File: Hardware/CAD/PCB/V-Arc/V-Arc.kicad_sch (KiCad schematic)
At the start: 0 parts

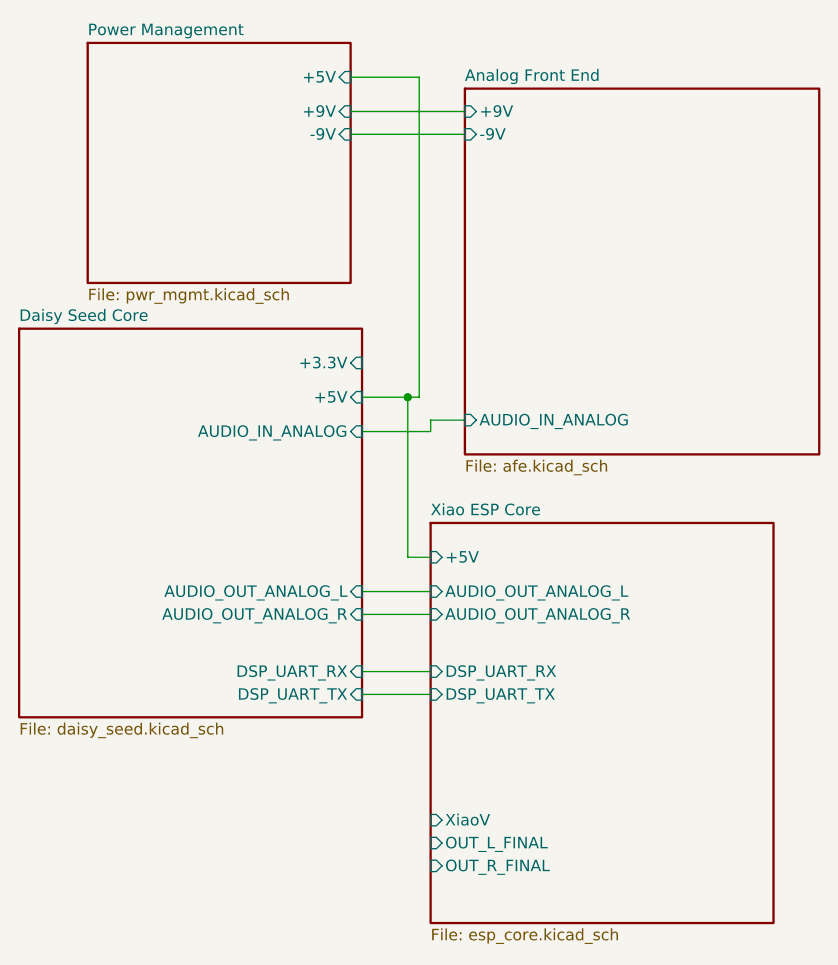
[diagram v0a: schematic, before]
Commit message: Assigned Footprints
-Swapped input jack to a switched one
-Assigned footprints for all items
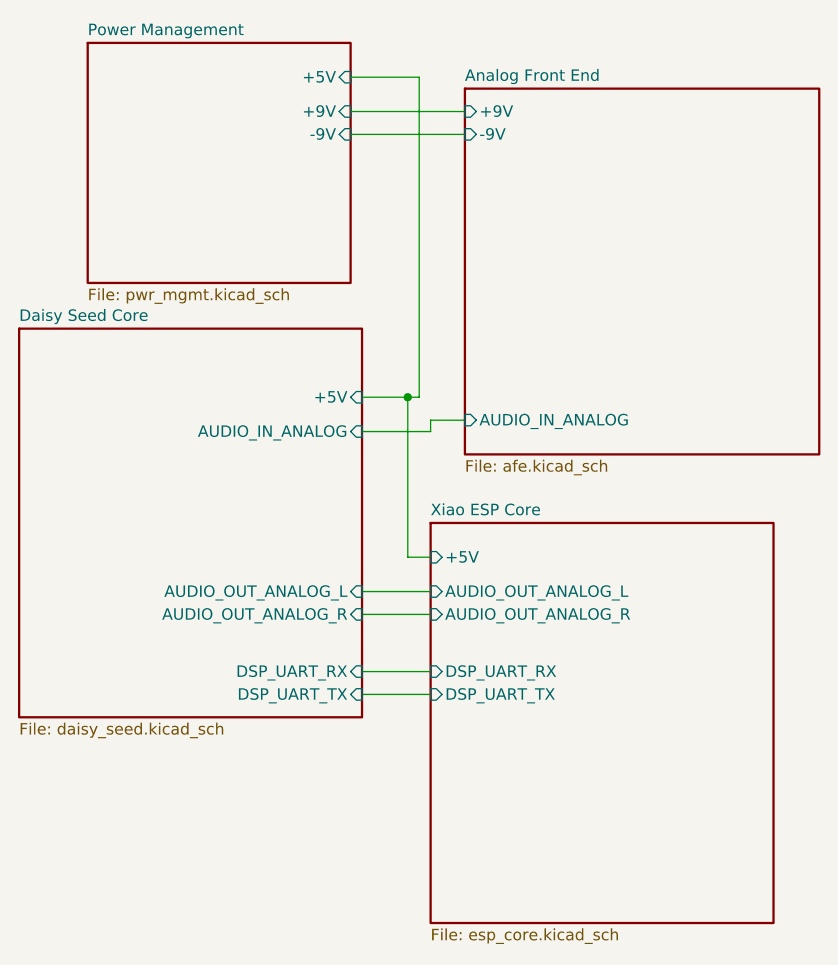
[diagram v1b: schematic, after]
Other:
- sheet Daisy Seed Core ports: added none; removed +3.3V
- sheet Xiao ESP Core ports: added none; removed OUT_L_FINAL, OUT_R_FINAL, XiaoV
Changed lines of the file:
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@@
-			)
-		)
-		(pin "XiaoV" input
-			(at 144.78 129.54 180)
-			(effects
-				(font
-					(size 1.27 1.27)
-				)
-				(justify left)
 			)
 		)
@@
 		(pin "AUDIO_OUT_ANALOG_R" input
 			(at 144.78 106.68 180)
-			(effects
-				(font
-					(size 1.27 1.27)
-				)
-				(justify left)
-			)
-		)
-		(pin "OUT_L_FINAL" input
-			(at 144.78 132.08 180)
-			(effects
-				(font
-					(size 1.27 1.27)
-				)
-				(justify left)
-			)
-		)
-		(pin "OUT_R_FINAL" input
-			(at 144.78 134.62 180)
 			(effects
 				(font
@@
 			)
 		)
-		(pin "+3.3V" input
-			(at 137.16 78.74 0)
-			(effects
-				(font
-					(size 1.27 1.27)
-					(color 251 255 253 1)
-				)
-				(justify right)
-			)
-		)
